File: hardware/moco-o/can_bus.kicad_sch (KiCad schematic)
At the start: 10 parts, among them J11 Conn_02x02_Top_Bottom, J12 Conn_02x02_Top_Bottom, U5 TJA1051T-3

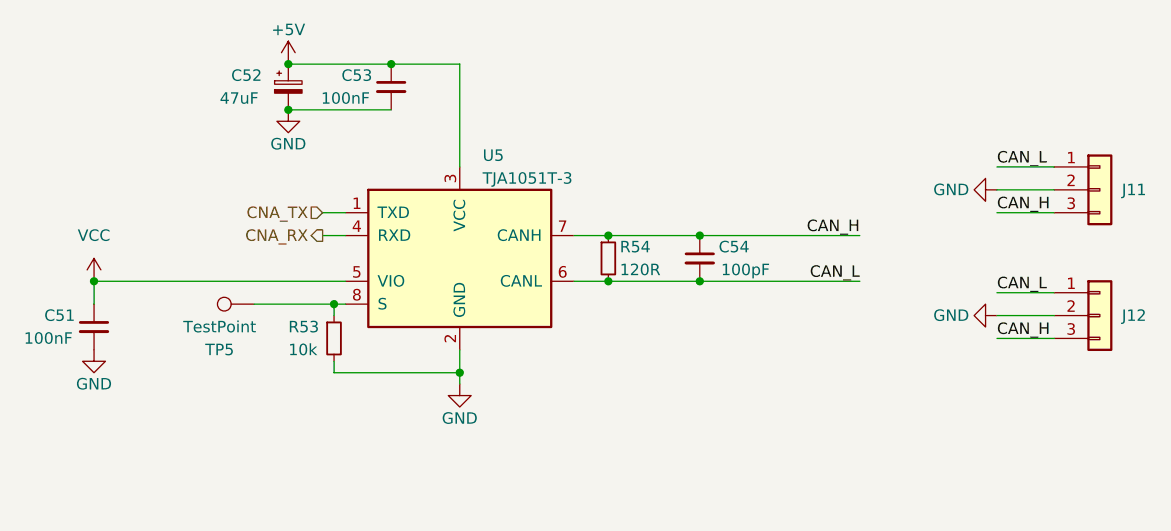
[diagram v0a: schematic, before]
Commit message: Change to DRV8323H
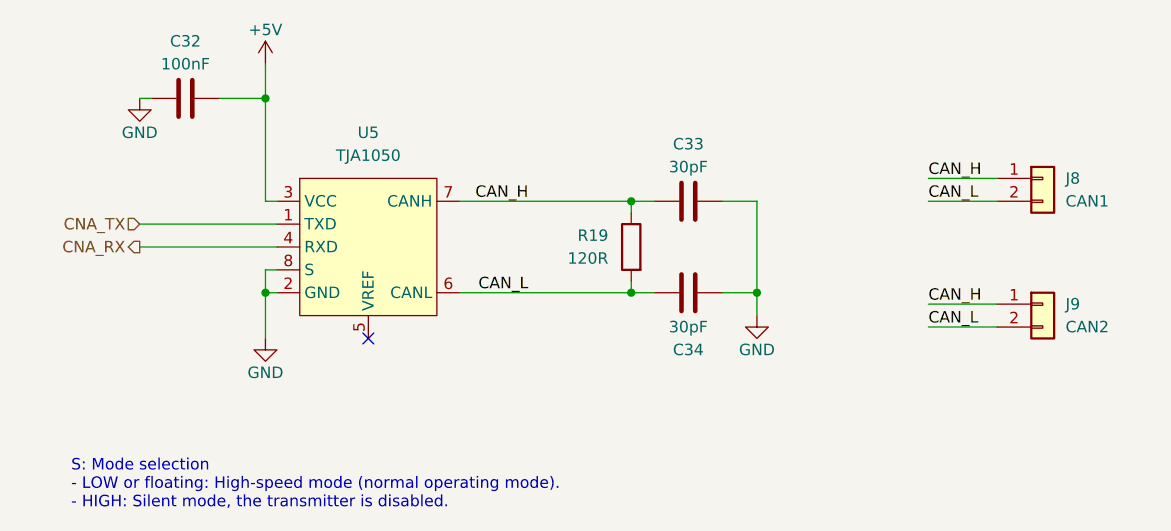
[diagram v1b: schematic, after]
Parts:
- removed C51, C53: 100nF, Capacitor_SMD:C_0402_1005Metric, symbol Device:C_Small
- removed C52: 47uF, Capacitor_SMD:C_0402_1005Metric, symbol Device:C_Polarized_Small
- removed C54: 100pF, Capacitor_SMD:C_0402_1005Metric, symbol Device:C_Small
- removed J11, J12: Conn_02x02_Top_Bottom, Connector_JST:JST_GH_SM03B-GHS-TB_1x03-1MP_P1.25mm_Horizontal, symbol Connector_Generic:Conn_01x03
- removed R53: 10k, Resistor_SMD:R_0402_1005Metric, symbol Device:R_Small
- removed R54: 120R, Resistor_SMD:R_0402_1005Metric, symbol Device:R_Small
- removed TP5: TestPoint, TestPoint:TestPoint_Pad_D2.0mm, symbol Connector:TestPoint
- removed U5: TJA1051T-3, Package_SO:SOIC-8_3.9x4.9mm_P1.27mm, symbol Interface_CAN_LIN:TJA1051T-3
- added C32: 100nF, Capacitor_SMD:C_0402_1005Metric, symbol Device:C
- added C33, C34: 30pF, Capacitor_SMD:C_0402_1005Metric, symbol Device:C
- added J8: CAN1, Connector_JST:JST_GH_BM02B-GHS-TBT_1x02-1MP_P1.25mm_Vertical, symbol Connector_Generic:Conn_01x02
- added J9: CAN2, Connector_JST:JST_GH_BM02B-GHS-TBT_1x02-1MP_P1.25mm_Vertical, symbol Connector_Generic:Conn_01x02
- added R19: 120R, Resistor_SMD:R_0402_1005Metric, symbol Device:R
- added U5: TJA1050, Package_SO:SOIC-8_3.9x4.9mm_P1.27mm, symbol moco:TJA1050
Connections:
- net +5V: now also C32.2, U5.3 (VCC)
- net CAN_H: now also C33.1, J8.1 (Pin_1), J9.1 (Pin_1), R19.1, U5.7 (CANH)
- net CAN_L: now also C34.1, J8.2 (Pin_2), J9.2 (Pin_2), R19.2, U5.6 (CANL)
- net CNA_RX: now also U5.4 (RXD)
- net CNA_TX: now also U5.1 (TXD)
- net GND: now also C32.1, C33.2, C34.2, U5.2 (GND), U5.8 (S)
- no-connect marks 0 -> 1
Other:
- note added: "S: Mode selection - LOW or floating: High-speed mode (normal operating mode). - HIGH: Silent mode, the transmitter is disabled."
